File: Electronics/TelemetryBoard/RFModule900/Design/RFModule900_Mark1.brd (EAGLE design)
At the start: 100 x 30 mm, 166 parts, among them T1 DC08-73, T2 DC08-73, U1 TPS2561, U2 TPS2561, U3 LM75B, U4 LTC5505, U5 LTC5505, U6 MCP4728, U7 ADC128D818, U8 MIC5504-3.3YM5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

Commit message: Simplified RX TX led driving
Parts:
- removed R16, R17: DNP, SparkFun-Resistors:0402-RES
- removed U$5: AO6602, RitLaunchInitiative:TSOP-6
- added C54: 0.1uF, SparkFun-Capacitors:0402-CAP
- added U$4: SN74LVC1G14, RitLaunchInitiative:SOT23-5
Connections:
- removed net N$35: D4.A, U$5.2
- removed net N$52: R17.1, U$5.3
- net 3.3V: now also C54.1, U$4.5; no longer R17.2, R5.1, U$5.4
- net BUFF_TR_SWITCH_CTL: now also D4.A, U$4.2; no longer R16.1, U$5.1
- net GND: now also C54.2, R5.2, U$4.3; no longer R16.2, U$5.5
- net N$33: now also D5.C, R5.1; no longer D5.A, R5.2
- net N$34: now also D5.A, U$4.4; no longer D5.C, U$5.6

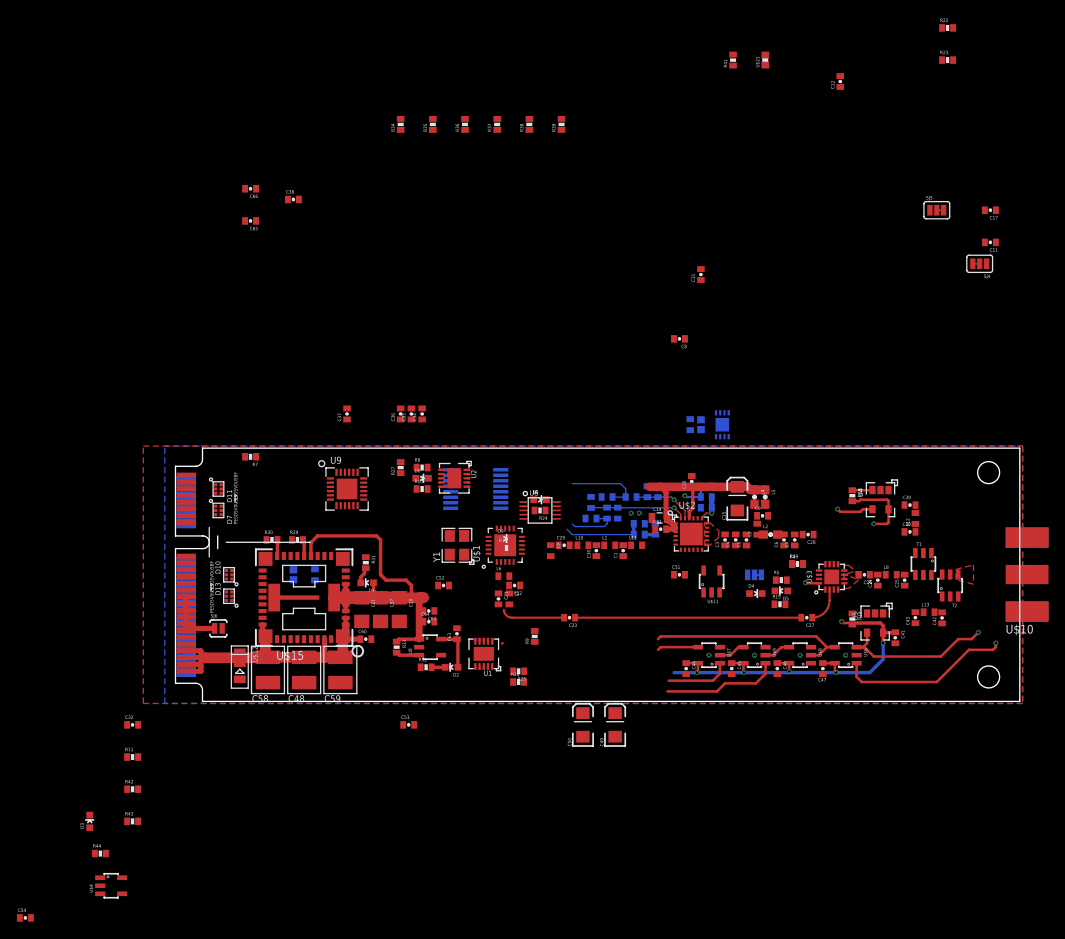
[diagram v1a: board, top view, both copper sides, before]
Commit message: reduced size of a couple logic gates
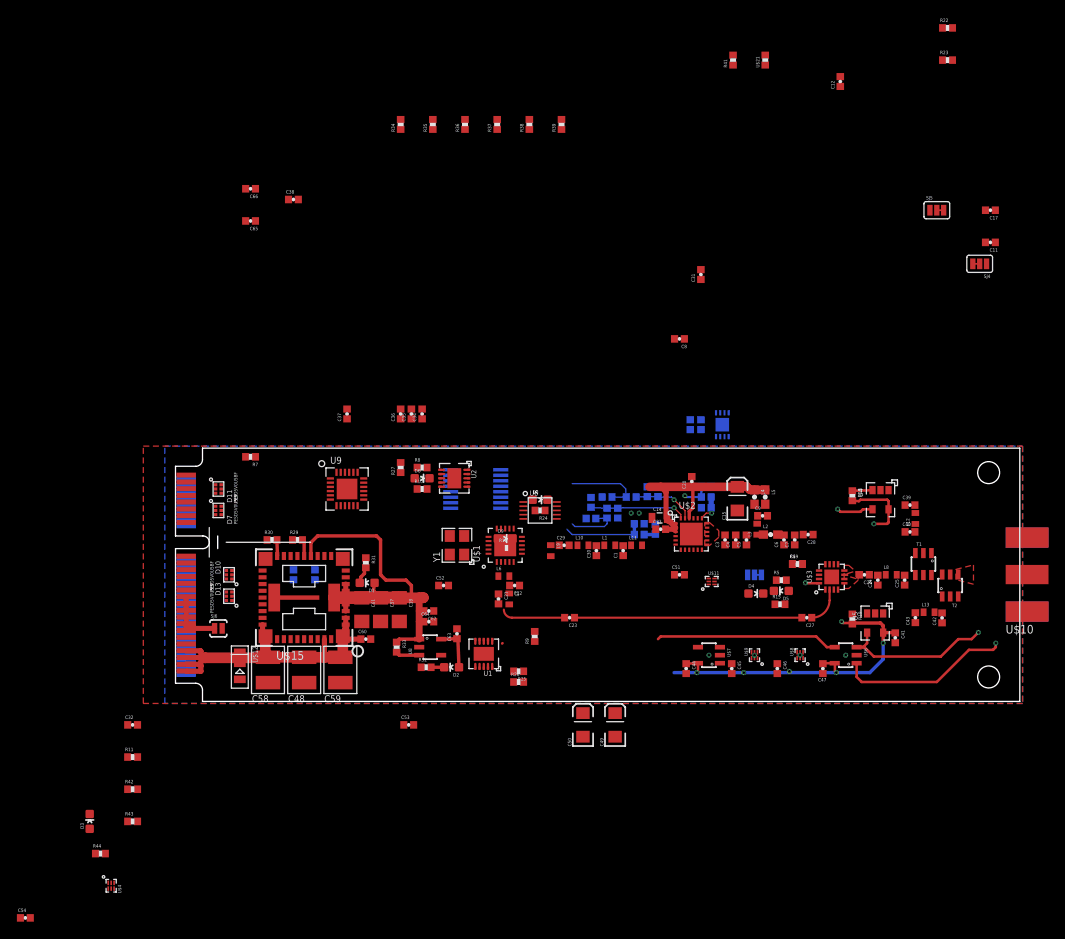
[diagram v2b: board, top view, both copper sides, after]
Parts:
- U$11, U$4, U$8: value SN74LVC1G14 -> SN74LVC1G14SOT23-56-SON; device RitLaunchInitiative:SOT23-5 -> RitLaunchInitiative:6-SON
- U$9: value SN74LVC1G32 -> SN74LVC1G326-SON6-SON; device RitLaunchInitiative:SOT23-5 -> RitLaunchInitiative:6-SON
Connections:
- net 3.3V: now also U$11.P$6, U$4.P$6, U$8.P$6, U$9.P$6; no longer U$11.5, U$4.5, U$8.5, U$9.5
- net BUFF_TR_SWITCH_CTL: now also U$11.P$4, U$4.P$2; no longer U$11.4, U$4.2
- net GND: now also U$11.P$3, U$4.P$3, U$8.P$3, U$9.P$3; no longer U$11.3, U$4.3, U$8.3, U$9.3
- net N$19: now also U$9.P$4; no longer U$9.4
- net N$3: now also U$8.P$4, U$9.P$2; no longer U$8.4, U$9.2
- net N$34: now also U$4.P$4; no longer U$4.4
- net PA_BREAKER_OVERRIDE: now also U$9.P$1; no longer U$9.1
- net TR_SWITCH_CTL: now also U$11.P$2; no longer U$11.2
- net VSWR_BREAKER_STATE: now also U$8.P$2; no longer U$8.2
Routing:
- net PA_BREAKER_OVERRIDE: track 13.7 -> 0.00 mm
- net PA_PWR_EN: track 7.65 -> 0.00 mm
- net PA_PWR_EN_BREAKER: track 4.86 -> 0.00 mm
- net 3.3V: track 92.4 -> 87.8 mm
- net N$3: track 3.19 -> 0.00 mm
- net N$19: track 3.19 -> 0.00 mm
- net VSWR_BREAKER_STATE: track 23.9 -> 21.6 mm
